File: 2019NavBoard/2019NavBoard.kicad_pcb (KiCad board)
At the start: 2 copper layers, 61 x 88.6 mm, 18 parts, among them J1 Conn_Coaxial, U1 TM4C129E_Launchpad, U5 FGPMMOPA6H

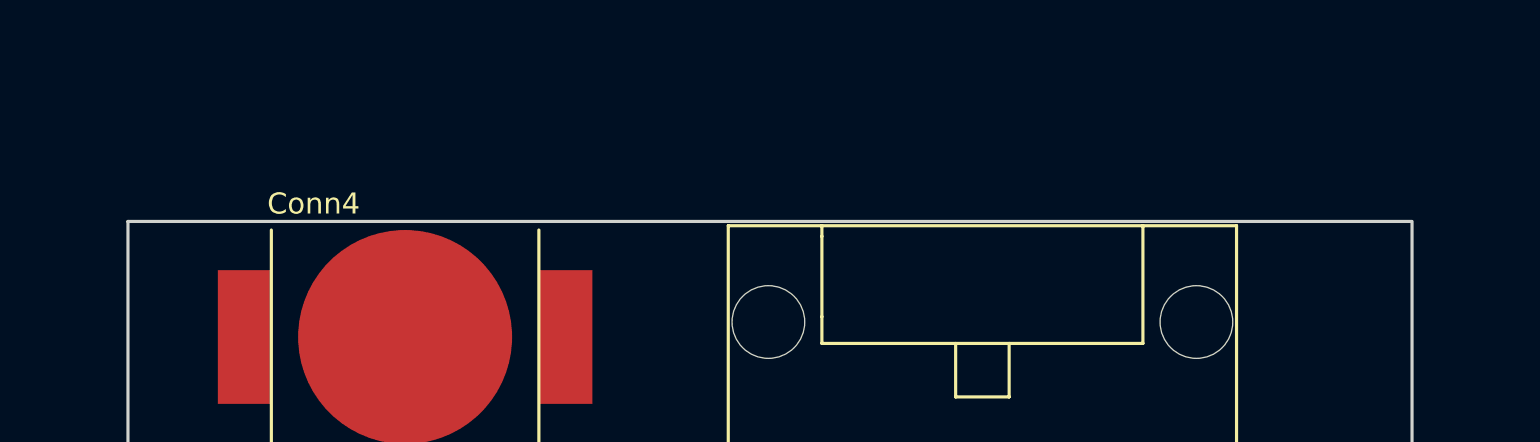
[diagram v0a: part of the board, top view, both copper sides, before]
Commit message: Fixed cut lines on PCB layout
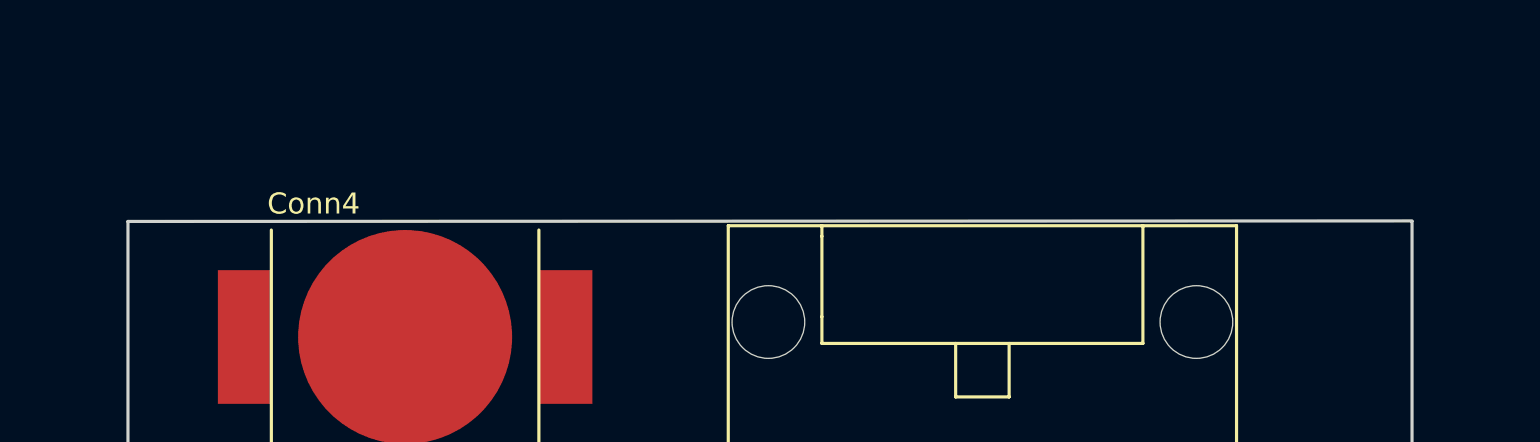
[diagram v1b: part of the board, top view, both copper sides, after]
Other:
- board size 61 x 88.6 mm -> 61 x 88.7 mm
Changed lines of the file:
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@@
       (xy 11.950441 -7.849394) (xy 11.953138 -7.835369) (xy 11.958067 -7.830303) (xy 11.962645 -7.830361)) (layer B.SilkS) (width 0.01))
   )
+  (gr_line (start 177.3174 55.6006) (end 116.3574 55.626) (layer Edge.Cuts) (width 0.15))
   (gr_text "GPS LED" (at 144.78 94.996) (layer F.SilkS)
     (effects (font (size 1.5 1.5) (thickness 0.3)))
@@
   (gr_arc (start 175.2854 96.52) (end 175.2854 98.552) (angle -90) (layer Edge.Cuts) (width 0.15))
   (gr_line (start 177.3174 55.626) (end 177.3174 96.52) (layer Edge.Cuts) (width 0.15))
-  (gr_line (start 177.292 55.626) (end 116.3574 55.626) (layer Edge.Cuts) (width 0.15))
   (gr_text "Board Power LED\n" (at 170.942 89.916) (layer F.SilkS)
     (effects (font (size 1 1) (thickness 0.25)))

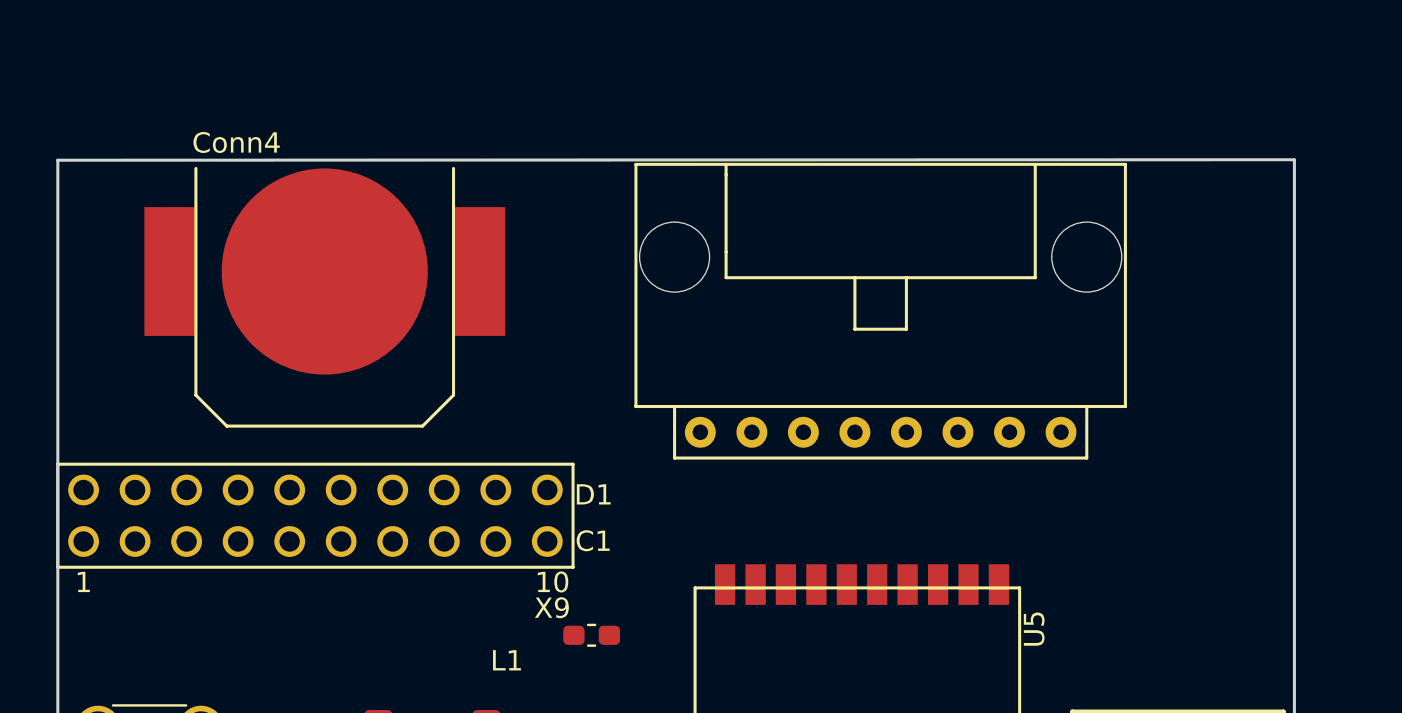
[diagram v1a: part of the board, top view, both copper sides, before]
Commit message: Fixed Errors and added a LIDAR
Some of the gobal labels had to be fixed and I added a LIDAR to the schematic. Also added some .txt files for pdr.
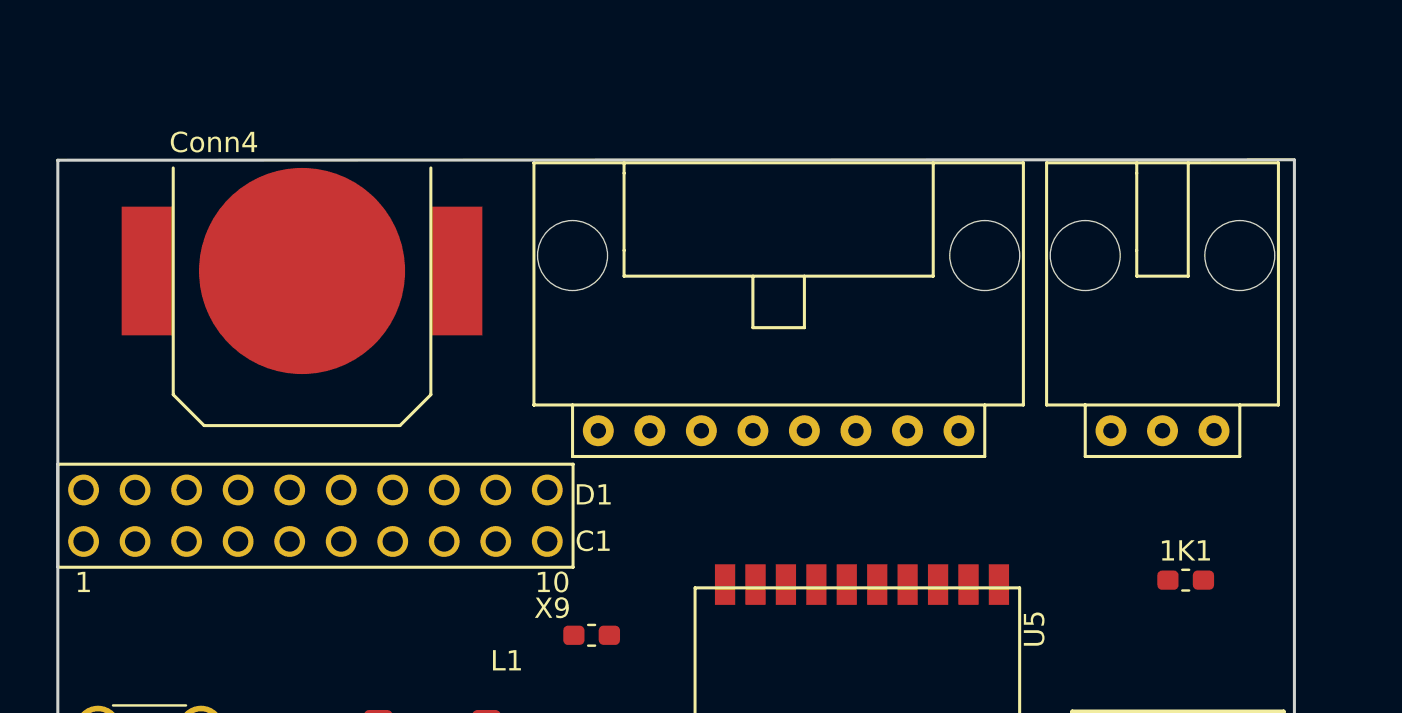
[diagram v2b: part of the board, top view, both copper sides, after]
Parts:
- added 1K1: R3, Resistor_SMD:R_0603_1608Metric_Pad1.05x0.95mm_HandSolder, F.Cu at (172.0, 76.3)
- added LIDAR1: Molex_SL_03, MRDT_Connectors:MOLEX_SL_03_Horizontal, F.Cu at (170.8, 69.0)
- R1: value 1k -> 1K
- U1: value TM4C129E_Launchpad -> ~
- moved Conn3 5.03 mm to (151.9, 69.0)
- moved Conn4 1.12 mm to (128.4, 61.1)
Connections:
- Conn3 pad 6: SDA -> SDA(0)
- Conn3 pad 7: SCL -> SCL(0)
- U1 pad PC4: Net-(U1-PadPC4) -> LIDAR_MONITOR
- U1 pad PC5: Net-(U1-PadPC5) -> LIDAR_TRIGGER
- U1 pad PF1: Net-(U1-PadPF1) -> (no net)
- U1 pad PF2: Net-(U1-PadPF2) -> (no net)
- U1 pad PF3: Net-(U1-PadPF3) -> (no net)
- U1 pad PG0: Net-(U1-PadPG0) -> (no net)
- U1 pad PL0: INT2 -> (no net)
- U1 pad PL1: INT1 -> (no net)
- U1 pad PL2: INTM -> (no net)
- U1 pad PL3: DRDYM -> (no net)
- U1 pad PL4: Net-(U1-PadPL4) -> (no net)
- U1 pad PL5: Net-(U1-PadPL5) -> (no net)

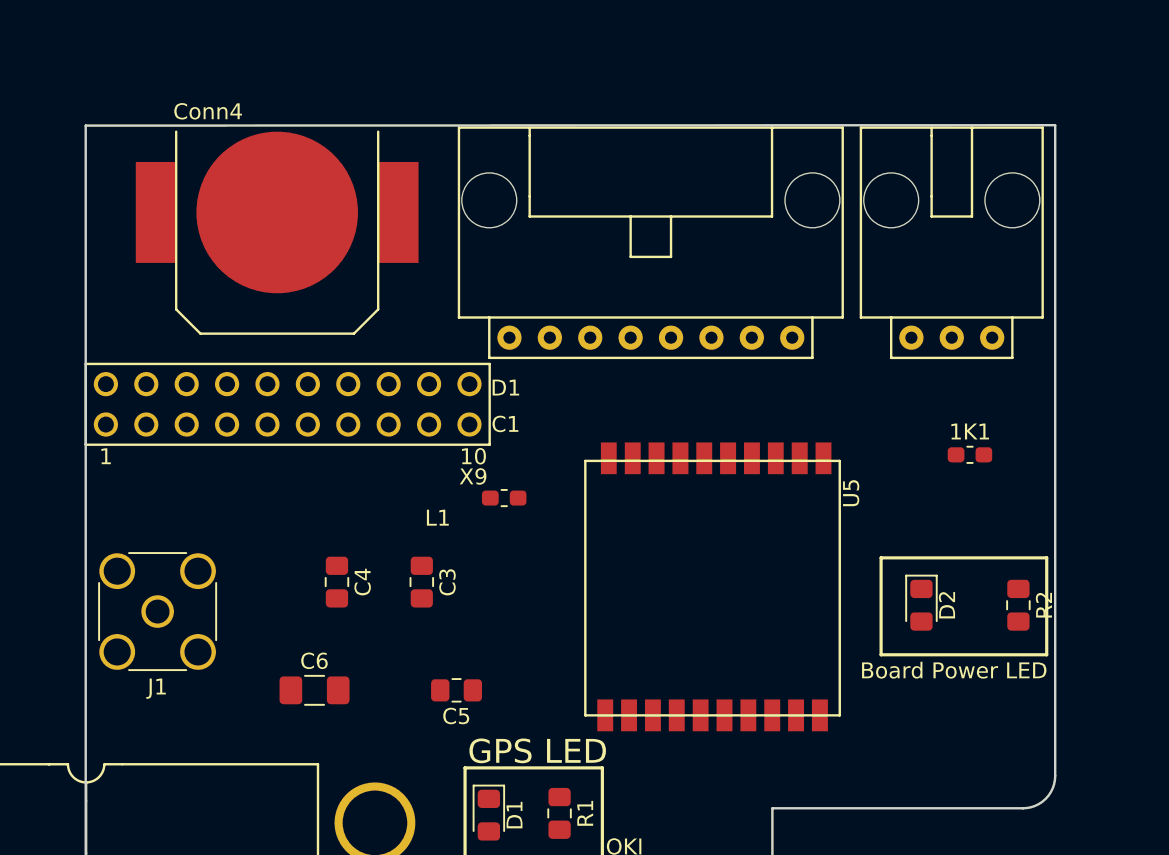
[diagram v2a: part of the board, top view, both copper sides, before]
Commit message: Added LIDAR 4SL
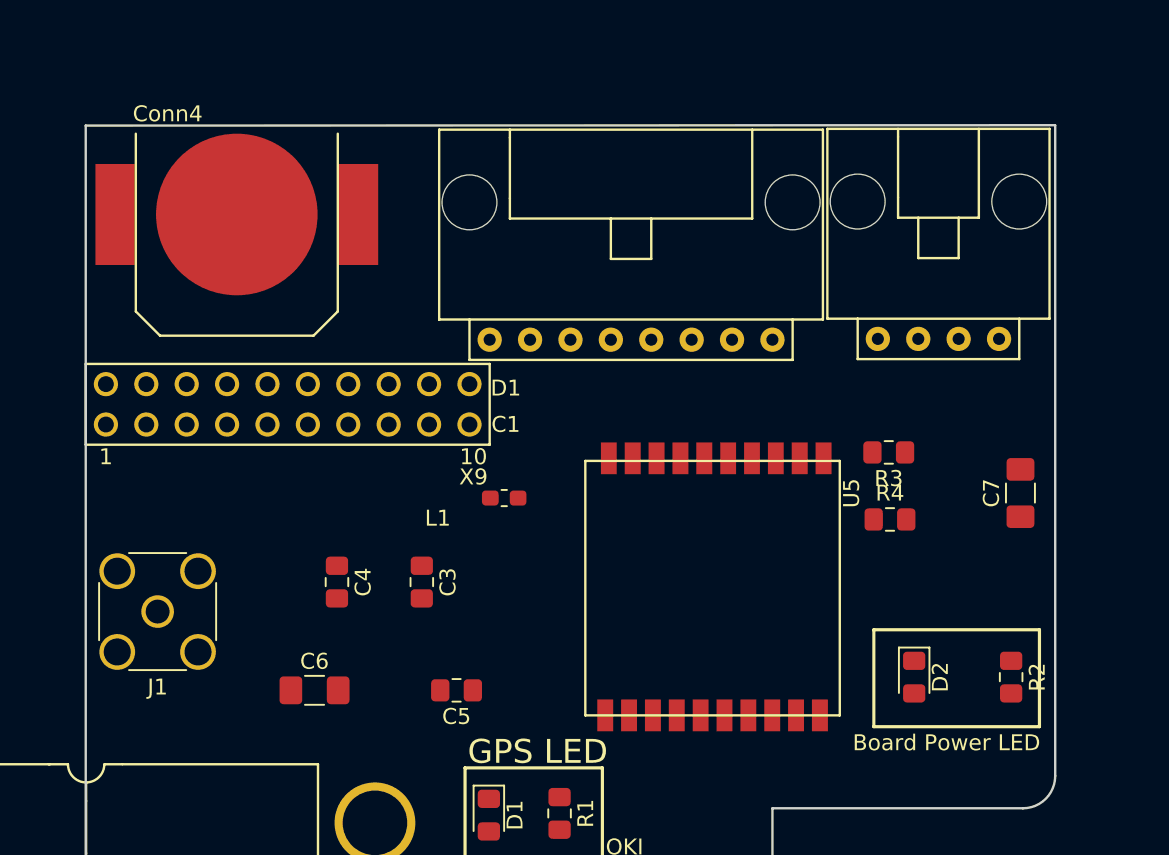
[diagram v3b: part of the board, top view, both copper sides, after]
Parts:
- removed 1K1: R3, Resistor_SMD:R_0603_1608Metric_Pad1.05x0.95mm_HandSolder
- added C7: 680uF, Capacitor_SMD:C_1206_3216Metric_Pad1.42x1.75mm_HandSolder, F.Cu at (175.1, 78.7)
- added R3: 4.7K, Resistor_SMD:R_0805_2012Metric_Pad1.15x1.40mm_HandSolder, F.Cu at (166.9, 76.2)
- added R4: 4.7K, Resistor_SMD:R_0805_2012Metric_Pad1.15x1.40mm_HandSolder, F.Cu at (166.9, 80.4)
- LIDAR1: value Molex_SL_03 -> Molex_SL_04; footprint MRDT_Connectors:MOLEX_SL_03_Horizontal -> MRDT_Connectors:MOLEX_SL_04_Horizontal
- moved D2 4.54 mm to (168.5, 90.3)
- moved R2 4.54 mm to (174.5, 90.3)
- moved Conn4 2.54 mm to (125.9, 61.2)
- moved Conn3 1.25 mm to (150.6, 69.1)
- moved LIDAR1 0.84 mm to (170.0, 69.0)
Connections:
- C1 pad 1: +5V -> LIDAR_MONITOR
- C2 pad 3: +5V -> LIDAR_MONITOR
- LIDAR1 pad 1: +5V -> GND
- LIDAR1 pad 2: LIDAR_MONITOR -> Net-(LIDAR1-Pad2)
- LIDAR1 pad 3: GND -> Net-(LIDAR1-Pad3)
- U1 pad +5V: +5V -> LIDAR_MONITOR
- U1 pad PC5: LIDAR_TRIGGER -> LIDAR_MONITOR
- U1 pad PC6: GPS_RX5 -> RX(7)
- U1 pad PC7: GPS_TX5 -> TX(7)

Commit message: Final PDR edits
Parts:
- moved Conn3 1.93 mm to (148.7, 69.1)
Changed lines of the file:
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@@
   )
   (module MRDT_Connectors:MOLEX_SL_08_Horizontal (layer F.Cu)
-    (at 150.6474 69.088)
+    (at 148.717 69.0626)
     (fp_text reference Conn3 (at -7.62 2.54) (layer F.SilkS) hide
       (effects (font (size 1 1) (thickness 0.15)))

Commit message: Changed indicators
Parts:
- added G***: LOGO, MRDT_Silkscreens:MRDT_Logo_20mm, F.Cu at (162.1, 130.3)
- moved D1 27.5 mm to (168.9, 95.2)
- moved R1 26.4 mm to (172.3, 95.2)
- moved G*** 12.2 mm to (147.3, 131.7), turned to 180 degrees
- moved C1 9.62 mm to (150.8, 99.6), turned to 180 degrees
- moved R2 3.46 mm to (172.3, 87.6)
- moved D2 2.71 mm to (169.0, 87.6)
- moved C2 0.72 mm to (144.5, 101.9)
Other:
- board text added: "GPS"
- board text added: "PWR"
- board text removed: "Board Power LED"
- board text removed: "GPS LED"

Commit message: PDR Ready
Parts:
- moved C5 2.72 mm to (137.5, 89.5), turned to 270 degrees
- moved C6 2.12 mm to (132.1, 89.5), turned to 90 degrees
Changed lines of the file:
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@@
     (pad_to_mask_clearance 0.2)
     (aux_axis_origin 0 0)
-    (visible_elements 7FFFFFFF)
+    (visible_elements 7FFFF7FF)
     (pcbplotparams
       (layerselection 0x010fc_ffffffff)
@@
   )
   (module Capacitor_SMD:C_0805_2012Metric_Pad1.15x1.40mm_HandSolder (layer F.Cu)
-    (at 139.6746 91.1352 180)
+    (at 137.5 89.5 270)
     (descr "Capacitor SMD 0805 (2012 Metric), square (rectangular) end terminal, IPC_7351 nominal with elongated pad for handsoldering. (Body size source: https://docs.google.com/spreadsheets/d/1BsfQQcO9C6DZCsRaXUlFlo91Tg2WpOkGARC1WS5S8t0/edit?usp=sharing), generated with kicad-footprint-generator")
     (tags "capacitor handsolder")
     (attr smd)
-    (fp_text reference C5 (at 0 -1.65 180) (layer F.SilkS)
-      (effects (font (size 1 1) (thickness 0.15)))
-    )
-    (fp_text value 1uF (at 0 1.65 180) (layer F.Fab)
+    (fp_text reference C5 (at 0 -1.65 270) (layer F.SilkS)
+      (effects (font (size 1 1) (thickness 0.15)))
+    )
+    (fp_text value 1uF (at 0 1.65 270) (layer F.Fab)
       (effects (font (size 1 1) (thickness 0.15)))
     )
@@
     (fp_line (start 1.85 -0.95) (end 1.85 0.95) (layer F.CrtYd) (width 0.05))
     (fp_line (start 1.85 0.95) (end -1.85 0.95) (layer F.CrtYd) (width 0.05))
-    (fp_text user %R (at 0 0 180) (layer F.Fab)
+    (fp_text user %R (at 0 0 270) (layer F.Fab)
       (effects (font (size 0.5 0.5) (thickness 0.08)))
     )
-    (pad 1 smd roundrect (at -1.025 0 180) (size 1.15 1.4) (layers F.Cu F.Paste F.Mask) (roundrect_rratio 0.217391)
+    (pad 1 smd roundrect (at -1.025 0 270) (size 1.15 1.4) (layers F.Cu F.Paste F.Mask) (roundrect_rratio 0.217391)
       (net 4 VBACKUP))
-    (pad 2 smd roundrect (at 1.025 0 180) (size 1.15 1.4) (layers F.Cu F.Paste F.Mask) (roundrect_rratio 0.217391)
+    (pad 2 smd roundrect (at 1.025 0 270) (size 1.15 1.4) (layers F.Cu F.Paste F.Mask) (roundrect_rratio 0.217391)
       (net 1 GND))
     (model ${KISYS3DMOD}/Capacitor_SMD.3dshapes/C_0805_2012Metric.wrl
@@
   )
   (module Capacitor_SMD:C_1206_3216Metric_Pad1.42x1.75mm_HandSolder (layer F.Cu)
-    (at 130.7449 91.1352)
+    (at 132.1 89.5 90)
     (descr "Capacitor SMD 1206 (3216 Metric), square (rectangular) end terminal, IPC_7351 nominal with elongated pad for handsoldering. (Body size source: http://www.tortai-tech.com/upload/download/2011102023233369053.pdf), generated with kicad-footprint-generator")
     (tags "capacitor handsolder")
     (attr smd)
-    (fp_text reference C6 (at 0 -1.82) (layer F.SilkS)
-      (effects (font (size 1 1) (thickness 0.15)))
-    )
-    (fp_text value 10uF (at 0 1.82) (layer F.Fab)
+    (fp_text reference C6 (at 0 -1.82 90) (layer F.SilkS)
+      (effects (font (size 1 1) (thickness 0.15)))
+    )
+    (fp_text value 10uF (at 0 1.82 90) (layer F.Fab)
       (effects (font (size 1 1) (thickness 0.15)))
     )
@@
     (fp_line (start 2.45 -1.12) (end 2.45 1.12) (layer F.CrtYd) (width 0.05))
     (fp_line (start 2.45 1.12) (end -2.45 1.12) (layer F.CrtYd) (width 0.05))
-    (fp_text user %R (at 0 0) (layer F.Fab)
+    (fp_text user %R (at 0 0 90) (layer F.Fab)
       (effects (font (size 0.8 0.8) (thickness 0.12)))
     )
-    (pad 1 smd roundrect (at -1.4875 0) (size 1.425 1.75) (layers F.Cu F.Paste F.Mask) (roundrect_rratio 0.175439)
+    (pad 1 smd roundrect (at -1.4875 0 90) (size 1.425 1.75) (layers F.Cu F.Paste F.Mask) (roundrect_rratio 0.175439)
       (net 2 "Net-(C2-Pad1)"))
-    (pad 2 smd roundrect (at 1.4875 0) (size 1.425 1.75) (layers F.Cu F.Paste F.Mask) (roundrect_rratio 0.175439)
+    (pad 2 smd roundrect (at 1.4875 0 90) (size 1.425 1.75) (layers F.Cu F.Paste F.Mask) (roundrect_rratio 0.175439)
       (net 1 GND))
     (model ${KISYS3DMOD}/Capacitor_SMD.3dshapes/C_1206_3216Metric.wrl

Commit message: Added Tracks
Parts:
- moved D1 4.03 mm to (172.8, 94.4), turned to 90 degrees
- moved D2 3.84 mm to (172.8, 87.4), turned to 90 degrees
- moved R1 3.01 mm to (169.4, 94.5), turned to 90 degrees
- moved R2 2.94 mm to (169.4, 87.4), turned to 90 degrees
- moved L1 0.35 mm to (142.6, 79.4)
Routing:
- net LIDAR_MONITOR: track 0.00 -> 102.5 mm, vias 0 -> 2
- net SCL(0): track 0.00 -> 59.5 mm
- net SDA(0): track 0.00 -> 54.3 mm
- net RX(7): track 0.00 -> 48.8 mm
- net Net-(J1-Pad1): track 0.00 -> 46.7 mm
- net +3V3: track 0.00 -> 44.7 mm
- net TX(7): track 0.00 -> 38.4 mm
- net Net-(C3-Pad1): track 0.00 -> 26.2 mm
- net Net-(C2-Pad1): track 0.00 -> 23.6 mm
- net GND: track 0.00 -> 21.3 mm
- net VBACKUP: track 0.00 -> 20.6 mm
- net Net-(R1-Pad1): track 0.00 -> 18.5 mm
- net Net-(LIDAR1-Pad3): track 0.00 -> 13.0 mm, vias 0 -> 1
- net Net-(LIDAR1-Pad2): track 0.00 -> 7.48 mm
- net Net-(D1-Pad2): track 0.00 -> 3.45 mm
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- added copper zone on B.Cu, net +3V3
- added copper zone on F.Cu, net GND
- removed copper zone on F.Cu, net +3V3
- removed copper zone on B.Cu, net GND
